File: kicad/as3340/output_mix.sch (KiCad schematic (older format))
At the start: 15 parts, among them U1 TL074, U5 DG442CY+, U6 AS3360, U8 DG442CY+

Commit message: start revision 0.3 of board
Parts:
- added R11: 560k, Resistor_SMD:R_0603_1608Metric, symbol Device:R
- added R2, R3, R39: 10k, Resistor_SMD:R_0603_1608Metric, symbol Device:R
- added R59: 12k, Resistor_SMD:R_0603_1608Metric, symbol Device:R
- R65, R66: footprint Resistor_SMD:R_1206_3216Metric -> Resistor_SMD:R_0603_1608Metric; LCSC Part C4410 -> (none)
- U6: symbol as3340-rescue:AS3360-Audio -> Audio:AS3360
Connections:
- wire segments 75 -> 83
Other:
- note added: "Passive mixing of various output waveforms\n"
- note removed: "Output level / scaling - Pulse and Saw"
- note removed: "TODO: check levels… this may be a bit odd"
- moved on the sheet: R10, R12, R13, R14, R5, R6, R65, R66, R7, R8, R9, U1A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

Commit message: routed v0.3
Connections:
- net MIX2_SAW_CTRL: now also U8.16; no longer U8.9
- net VCO_SAW: now also U8.14; no longer U8.11
- net at R14.1: now also U8.15; no longer U8.10
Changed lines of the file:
@@
 $Comp
 L Analog_Switch:DG441xJ U?
-U 3 1 626F5A8E
+U 4 1 626F5A8E
 P 9200 7500
 AR Path="/626F5A8E" Ref="U?"  Part="3"
-AR Path="/6269DD41/626F5A8E" Ref="U8"  Part="3"
+AR Path="/6269DD41/626F5A8E" Ref="U8"  Part="4"
 F 0 "U8" H 9200 7675 50  0000 C CNN
 F 1 "DG442CY+" H 9200 7766 50  0000 C CNN
@@
 F 3 "https://datasheets.maximintegrated.com/en/ds/DG441-DG442.pdf" H 9200 7500 50  0001 C CNN
 F 4 "DG442CY+-ND" H 9200 7500 50  0001 C CNN "Digikey"
-	3    9200 7500
+	4    9200 7500
 	-1   0    0    1
 $EndComp

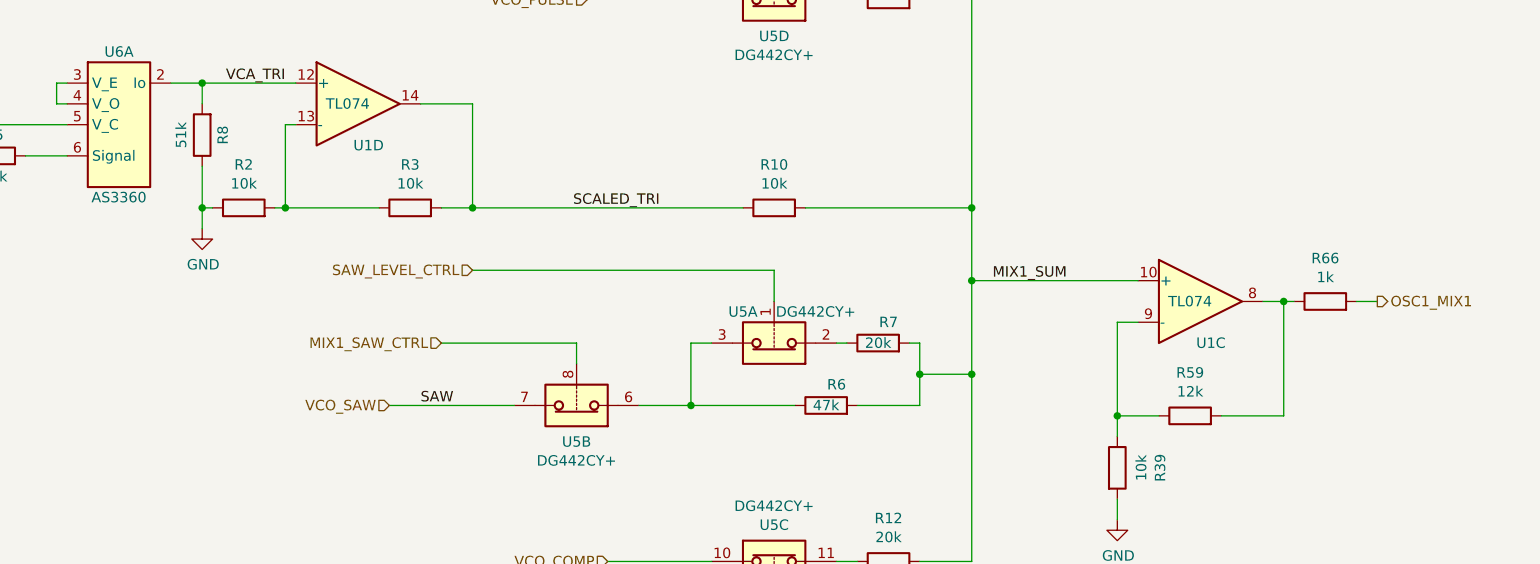
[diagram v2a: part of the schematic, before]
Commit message: added id chip and some tweaks
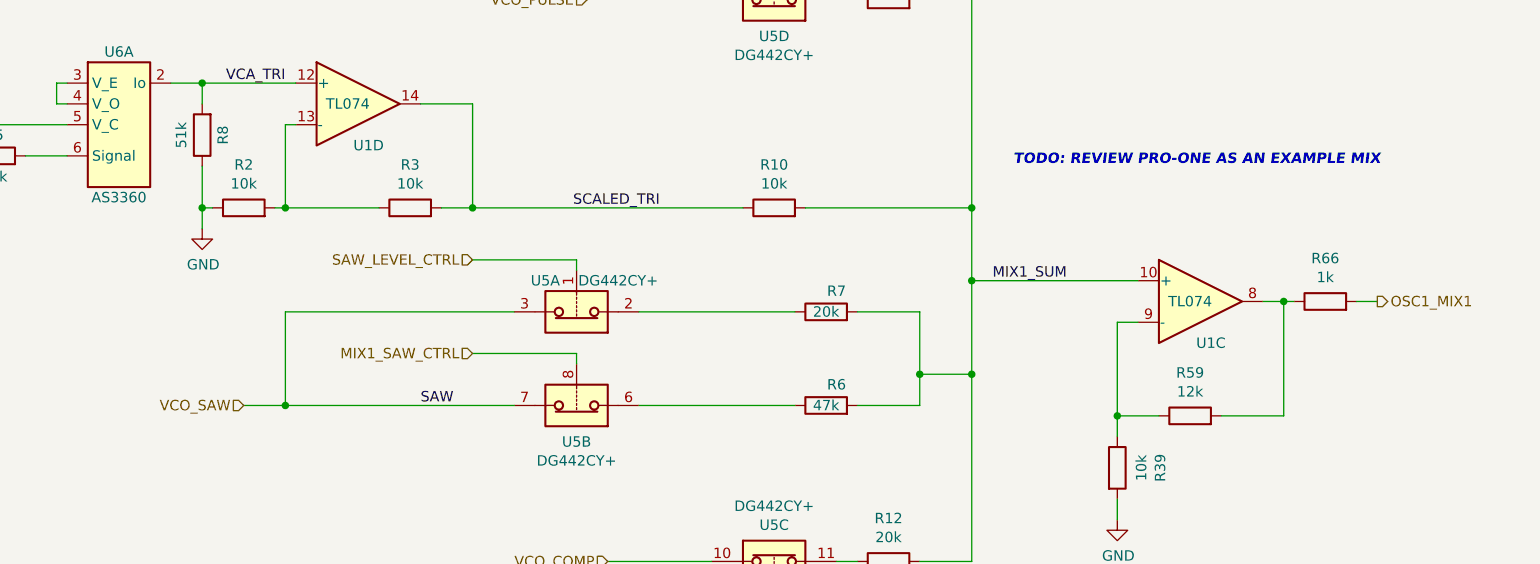
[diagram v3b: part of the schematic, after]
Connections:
- net VCO_SAW: now also U5.3
- net at R6.1, U5.6: no longer U5.3
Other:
- note added: "TODO: REVIEW PRO-ONE AS AN EXAMPLE MIX"
- moved on the sheet: R7, U5A
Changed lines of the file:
@@
 $EndDescr
 Wire Wire Line
-	8150 4500 7500 4500
+	8150 4550 7650 4550
 Wire Wire Line
 	8500 2450 9100 2450
@@
 	9100 2450 9100 2650
 Wire Wire Line
-	8150 4600 8150 4500
+	8150 4600 8150 4550
 $Comp
 L Device:R R?
@@
 L Analog_Switch:DG441xJ U?
 U 1 1 626F5AD5
-P 9100 4500
+P 8150 4350
 AR Path="/626F5AD5" Ref="U?"  Part="1"
 AR Path="/6269DD41/626F5AD5" Ref="U5"  Part="1"
-F 0 "U5" H 9250 4350 50  0000 C CNN
-F 1 "DG442CY+" H 8900 4350 50  0000 C CNN
-F 2 "Package_SO:SOIC-16_3.9x9.9mm_P1.27mm" H 9100 4400 50  0001 C CNN
-F 3 "https://datasheets.maximintegrated.com/en/ds/DG441-DG442.pdf" H 9100 4500 50  0001 C CNN
-F 4 "DG442CY+-ND" H 9100 4500 50  0001 C CNN "Digikey"
-	1    9100 4500
+F 0 "U5" H 8300 4200 50  0000 C CNN
+F 1 "DG442CY+" H 7950 4200 50  0000 C CNN
+F 2 "Package_SO:SOIC-16_3.9x9.9mm_P1.27mm" H 8150 4250 50  0001 C CNN
+F 3 "https://datasheets.maximintegrated.com/en/ds/DG441-DG442.pdf" H 8150 4350 50  0001 C CNN
+F 4 "DG442CY+-ND" H 8150 4350 50  0001 C CNN "Digikey"
+	1    8150 4350
 	-1   0    0    1
 $EndComp
@@
 L Device:R R?
 U 1 1 626F5B03
-P 9600 4500
+P 9350 4350
 AR Path="/61E1D4AE/626F5B03" Ref="R?"  Part="1"
 AR Path="/626F5B03" Ref="R?"  Part="1"
 AR Path="/6269DD41/626F5B03" Ref="R7"  Part="1"
-F 0 "R7" V 9700 4450 50  0000 C CNN
-F 1 "20k" V 9600 4500 50  0000 C CNN
-F 2 "Resistor_SMD:R_0603_1608Metric" V 9530 4500 50  0001 C CNN
-F 3 "~" H 9600 4500 50  0001 C CNN
-F 4 "C4184" H 9600 4500 50  0001 C CNN "LCSC Part"
-	1    9600 4500
+F 0 "R7" V 9450 4300 50  0000 C CNN
+F 1 "20k" V 9350 4350 50  0000 C CNN
+F 2 "Resistor_SMD:R_0603_1608Metric" V 9280 4350 50  0001 C CNN
+F 3 "~" H 9350 4350 50  0001 C CNN
+F 4 "C4184" H 9350 4350 50  0001 C CNN "LCSC Part"
+	1    9350 4350
 	0    -1   -1   0
 $EndComp
@@
 	8150 7500 8900 7500
 Wire Wire Line
-	7250 4800 7850 4800
+	6550 4800 6750 4800
 Wire Wire Line
 	8200 6750 8900 6750
@@
 	11900 4300 12000 4300
 Wire Wire Line
-	7650 4150 9100 4150
-Wire Wire Line
-	9400 4500 9450 4500
+	7650 4100 8150 4100
+Wire Wire Line
+	8450 4350 9200 4350
 Text HLabel 8200 2850 0    50   Input ~ 0
 VCO_PULSE
-Text HLabel 7250 4800 0    50   Input ~ 0
+Text HLabel 6550 4800 0    50   Input ~ 0
 VCO_SAW
-Text HLabel 7650 4150 0    50   Input ~ 0
+Text HLabel 7650 4100 0    50   Input ~ 0
 SAW_LEVEL_CTRL
 Text HLabel 8300 5550 0    50   Input ~ 0
@@
 Text HLabel 8500 2450 0    50   Input ~ 0
 MIX1_PULSE_CTRL
-Text HLabel 7500 4500 0    50   Input ~ 0
-MIX1_SAW_CTRL
 Text HLabel 8750 5850 0    50   Input ~ 0
 MIX1_COMP_OSC2_CTRL
@@
 	10050 4200 10050 4650
 Wire Wire Line
-	8450 4800 8700 4800
-Wire Wire Line
-	9100 4150 9100 4300
-Wire Wire Line
-	8700 4800 8700 4500
-Wire Wire Line
-	8700 4500 8800 4500
-Connection ~ 8700 4800
-Wire Wire Line
-	8700 4800 9200 4800
+	8150 4100 8150 4150
 Wire Wire Line
 	9500 4800 9800 4800
@@
 	10050 4650 10050 5550
 Wire Wire Line
-	9750 4500 9800 4500
-Wire Wire Line
-	9800 4500 9800 4650
+	9500 4350 9800 4350
+Wire Wire Line
+	9800 4350 9800 4650
 Connection ~ 9800 4650
 Wire Wire Line
@@
 Text Notes 7400 2050 0    50   ~ 0
 Passive mixing of various output waveforms\n
+Wire Wire Line
+	8450 4800 9200 4800
+Text HLabel 7650 4550 0    50   Input ~ 0
+MIX1_SAW_CTRL
+Wire Wire Line
+	6750 4800 6750 4350
+Wire Wire Line
+	6750 4350 7850 4350
+Connection ~ 6750 4800
+Wire Wire Line
+	6750 4800 7850 4800
+Text Notes 10250 3650 0    50   Italic 10
+TODO: REVIEW PRO-ONE AS AN EXAMPLE MIX
 $EndSCHEMATC

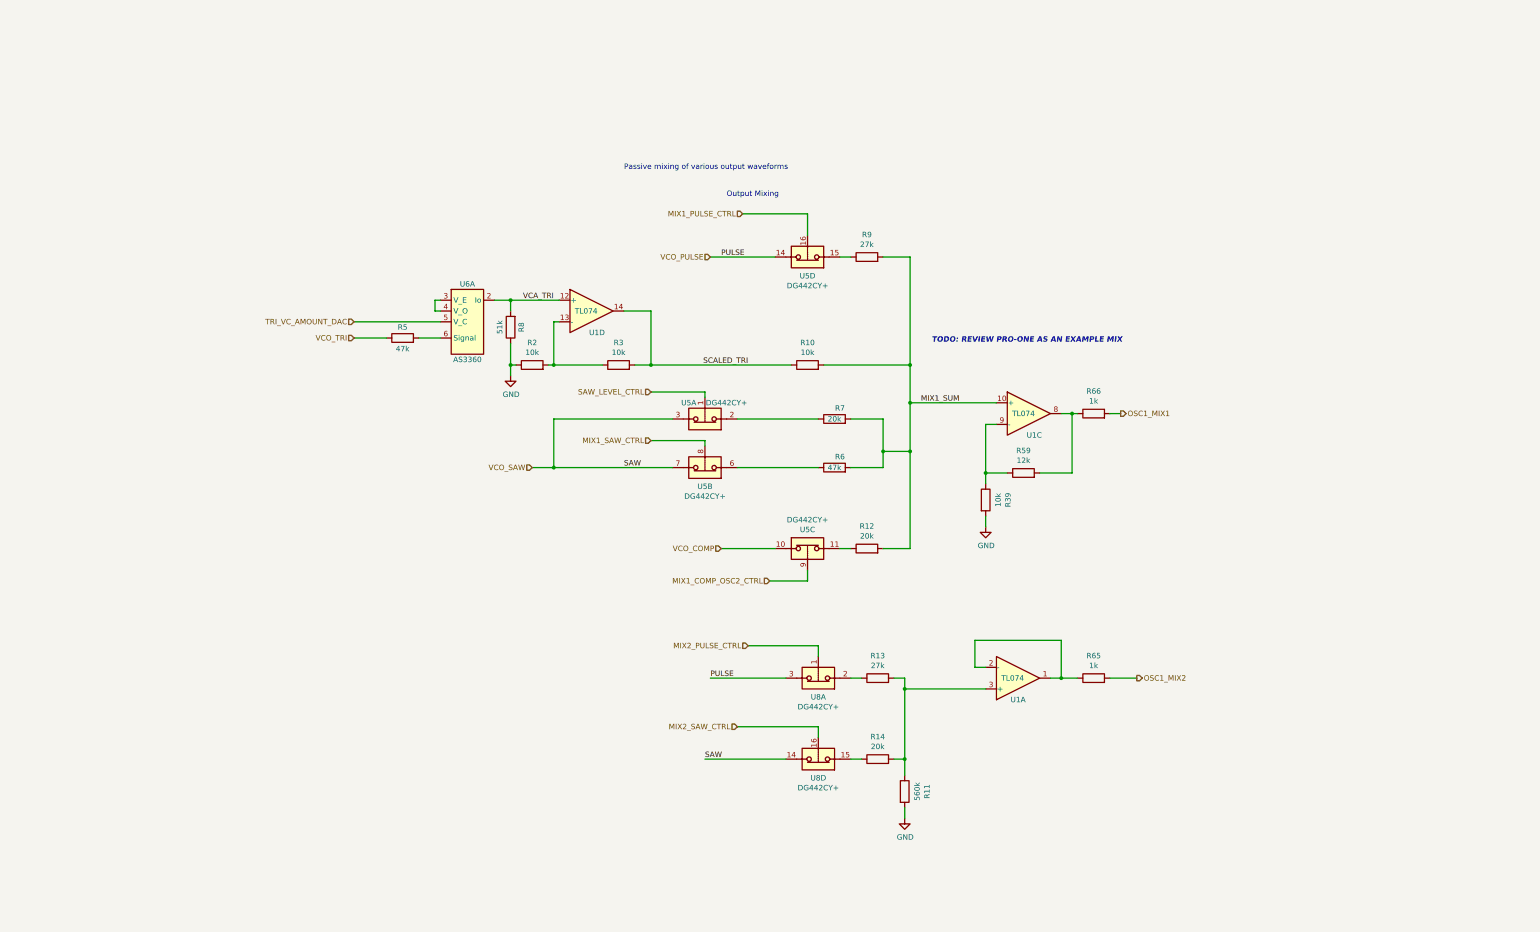
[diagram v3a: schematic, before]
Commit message: added routing/mix to compare contemporary designs
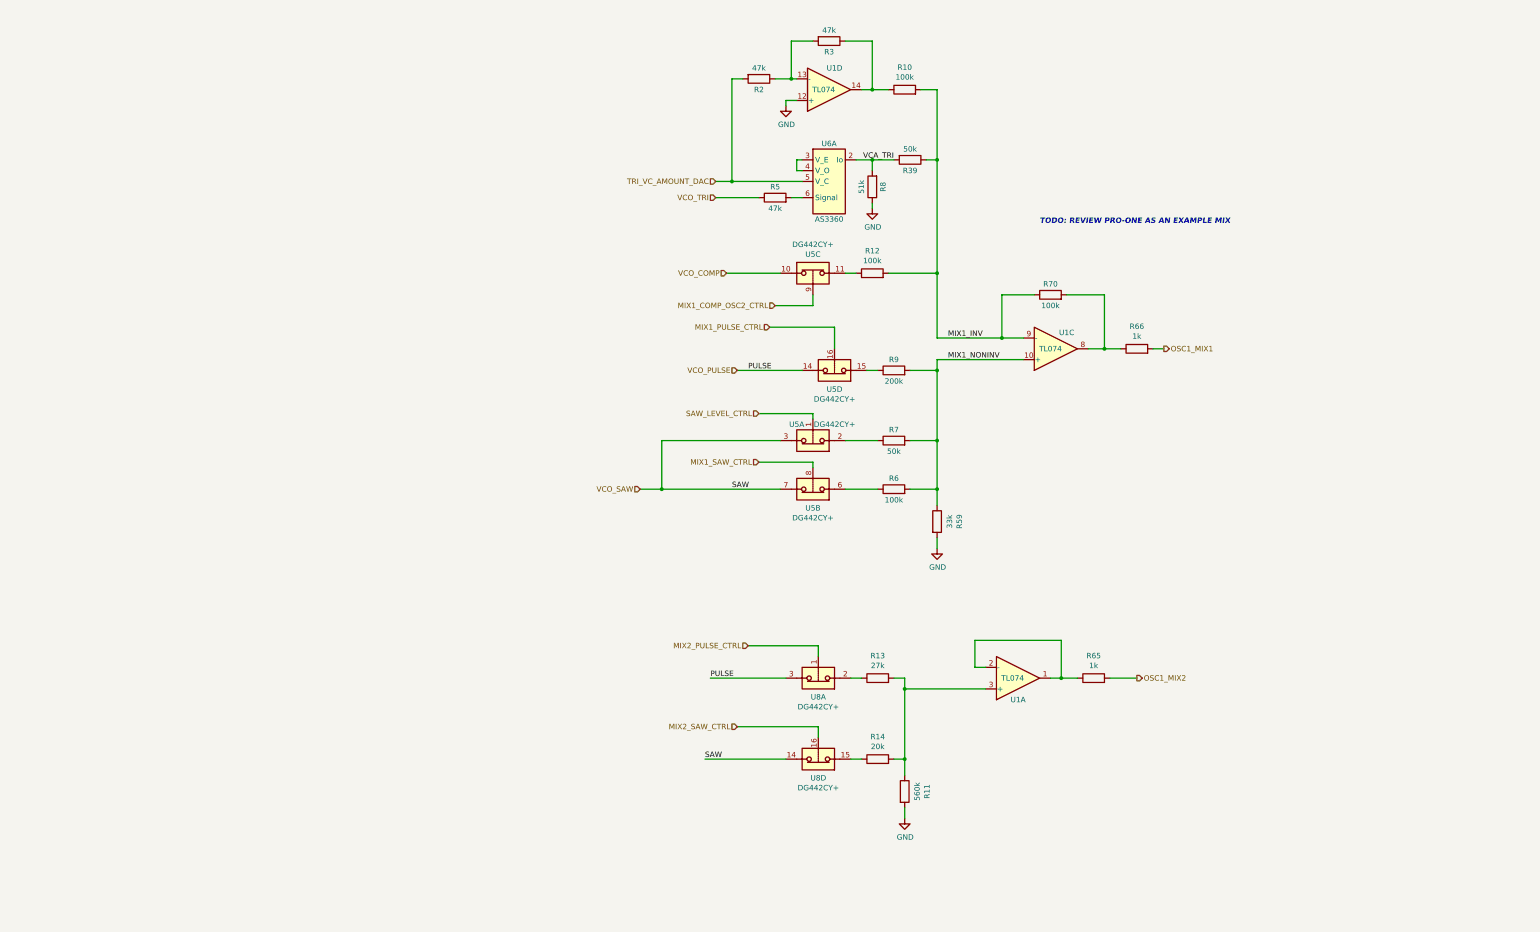
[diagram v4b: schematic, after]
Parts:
- added R70: 100k, Resistor_SMD:R_0603_1608Metric, symbol Device:R
- R10: value 10k -> 100k; LCSC Part C25804 -> \\
- R12: value 20k -> 100k; LCSC Part C4184 -> \\
- R2, R3: value 10k -> 47k; LCSC Part C25804 -> C25819
- R39: value 10k -> 50k
- R59: value 12k -> 33k
- R6: value 47k -> 100k; LCSC Part C25819 -> (none)
- R7: value 20k -> 50k; LCSC Part C4184 -> (none)
- R9: value 27k -> 200k; LCSC Part C22967 -> (none)
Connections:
- net GND: now also R59.2, U1.12 (+); no longer R2.1, R39.2
- net TRI_VC_AMOUNT_DAC: now also R2.2
- net VCA_TRI: now also R39.2; no longer U1.12 (+)
- net at R66.1, U1.8: now also R70.2; no longer R59.2
- net MIX1_INV: now reaches R39.1, U1.9 (-)
- net MIX1_INV: now also R10.2, R12.2, R70.1; no longer R59.1
- net MIX1_SUM renamed MIX1_NONINV
- net MIX1_NONINV: now also R59.1; no longer R10.2, R12.2
- net SCALED_TRI: no longer names the net of R10.1, U1.14
- net SCALED_TRI: now also R3.1; no longer R3.2
- new net: R2.1, R3.2, U1.13 (-)
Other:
- note removed: "Output Mixing"
- note removed: "Passive mixing of various output waveforms\n"
- moved on the sheet: R12, R5, R6, R66, R7, R8, R9, U1C, U1D, U5A, U5B, U5C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

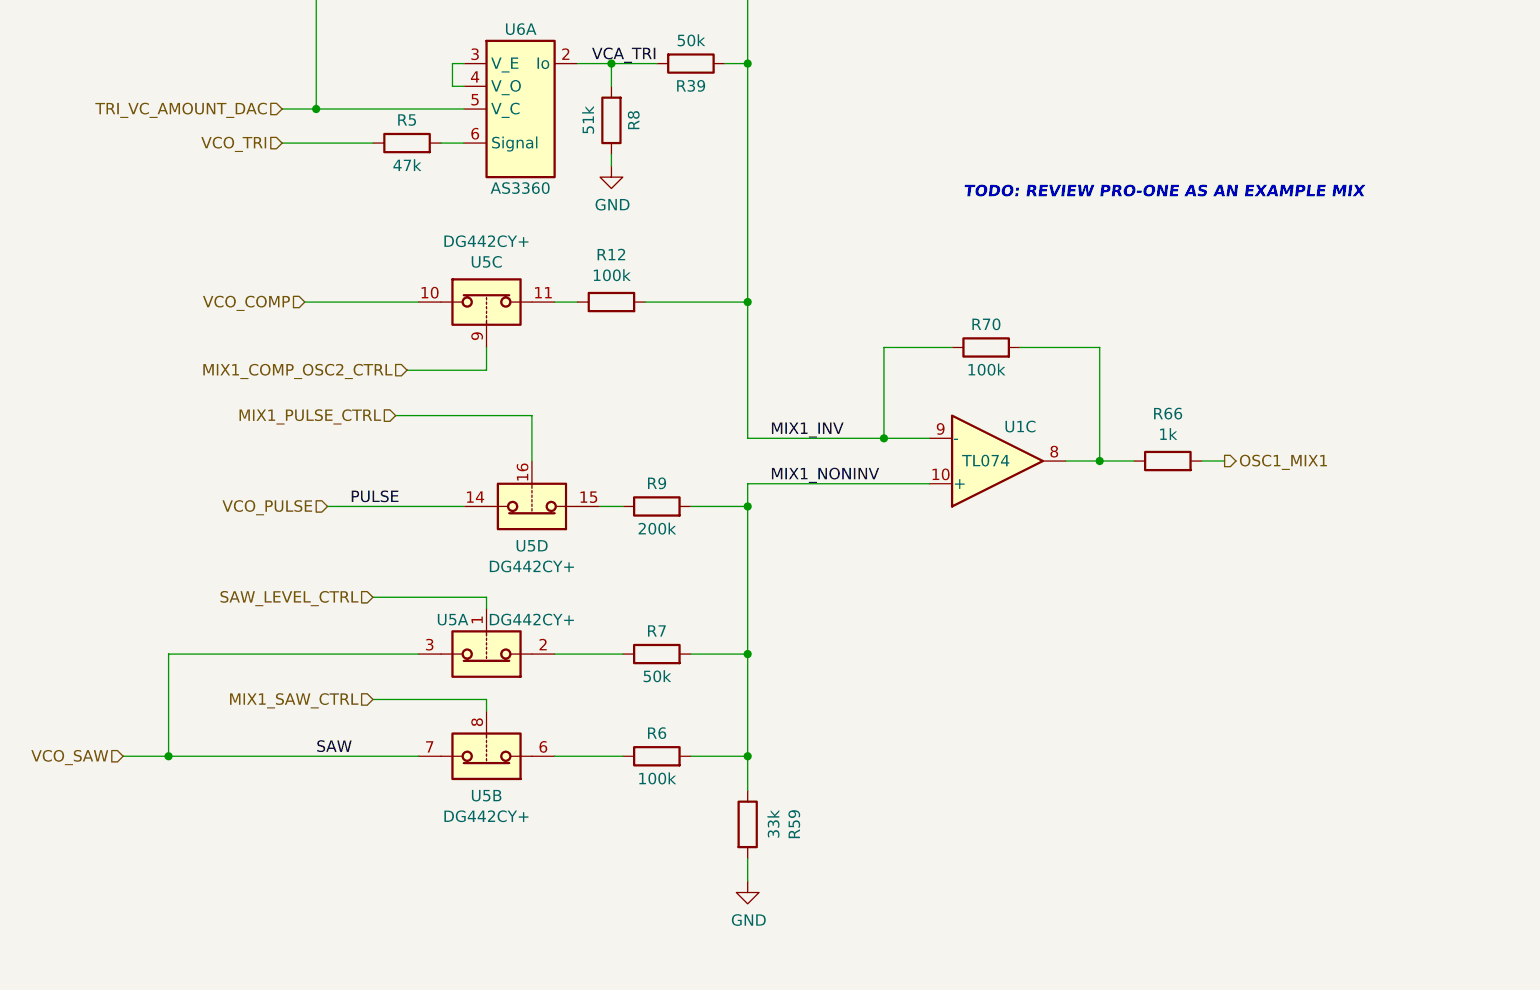
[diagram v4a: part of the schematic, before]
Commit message: rework output stage
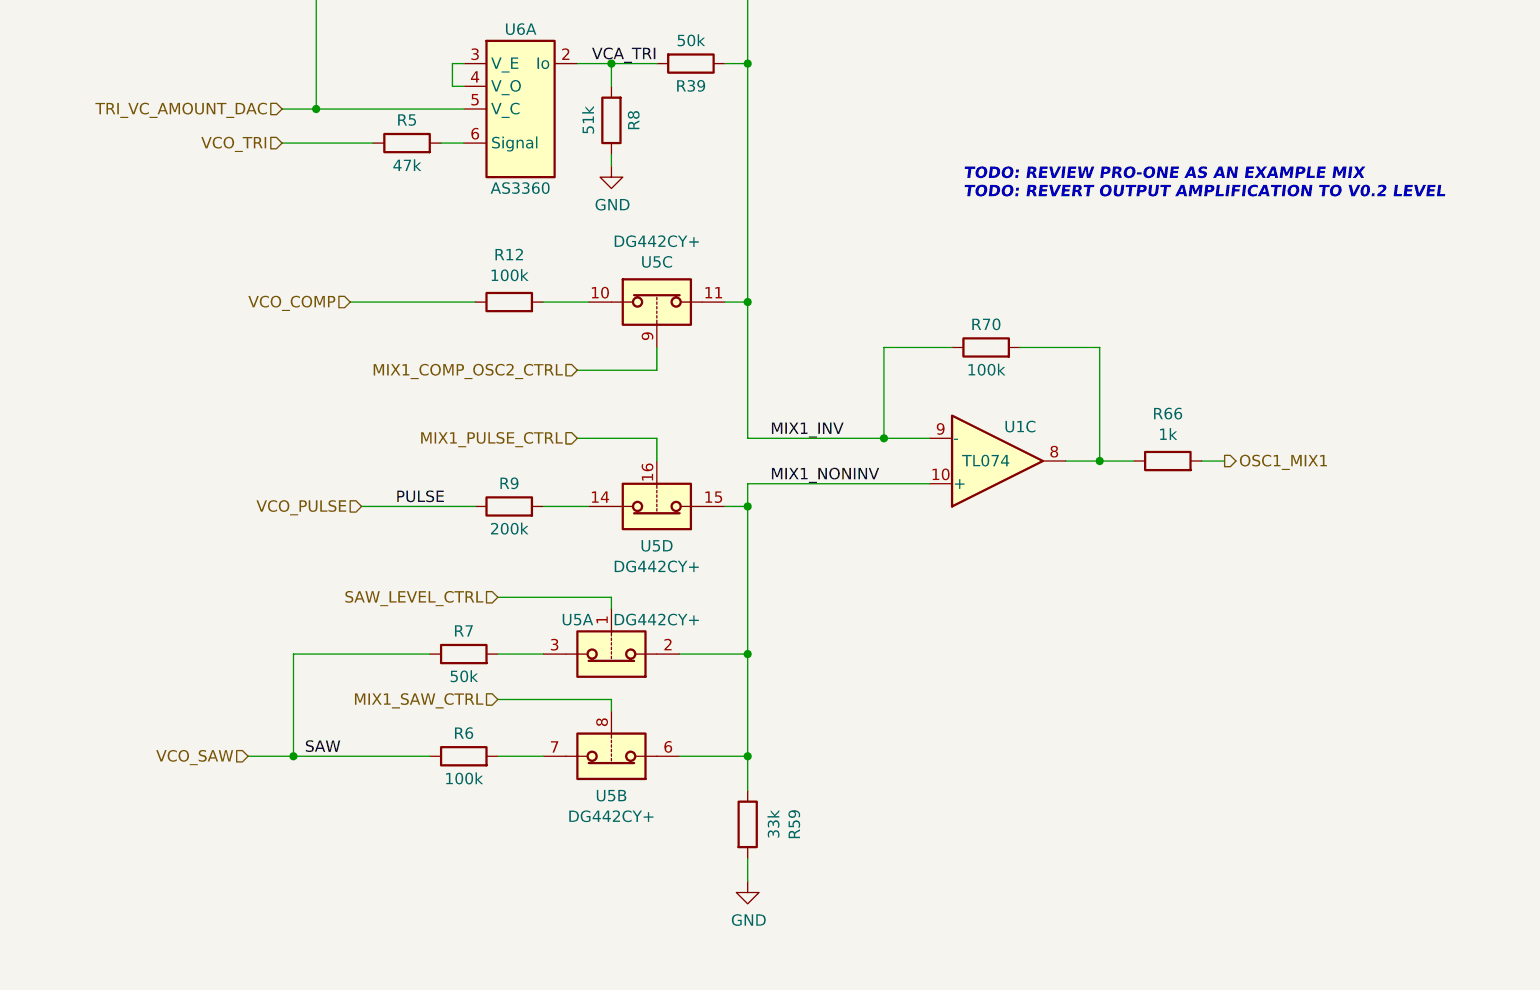
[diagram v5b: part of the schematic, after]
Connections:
- net MIX1_INV: now also U5.11; no longer R12.2
- net MIX1_NONINV: now also U5.15, U5.2, U5.6; no longer R6.2, R7.2, R9.2
- net VCO_COMP: now also R12.1; no longer U5.10
- net VCO_PULSE: now also R9.1; no longer U5.14
- net VCO_SAW: now also R6.1, R7.1; no longer U5.3, U5.7
- new net: R9.2, U5.14
- new net: R12.2, U5.10
- new net: R6.2, U5.7
- new net: R7.2, U5.3
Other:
- note added: "TODO: REVIEW PRO-ONE AS AN EXAMPLE MIX\nTODO: REVERT OUTPUT AMPLIFICATION TO V0.2 LEVEL"
- note removed: "TODO: REVIEW PRO-ONE AS AN EXAMPLE MIX"
- moved on the sheet: R12, R6, R7, R9, U5A, U5B, U5C, U5D
